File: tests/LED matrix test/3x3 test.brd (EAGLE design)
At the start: 100 x 80 mm, 21 parts

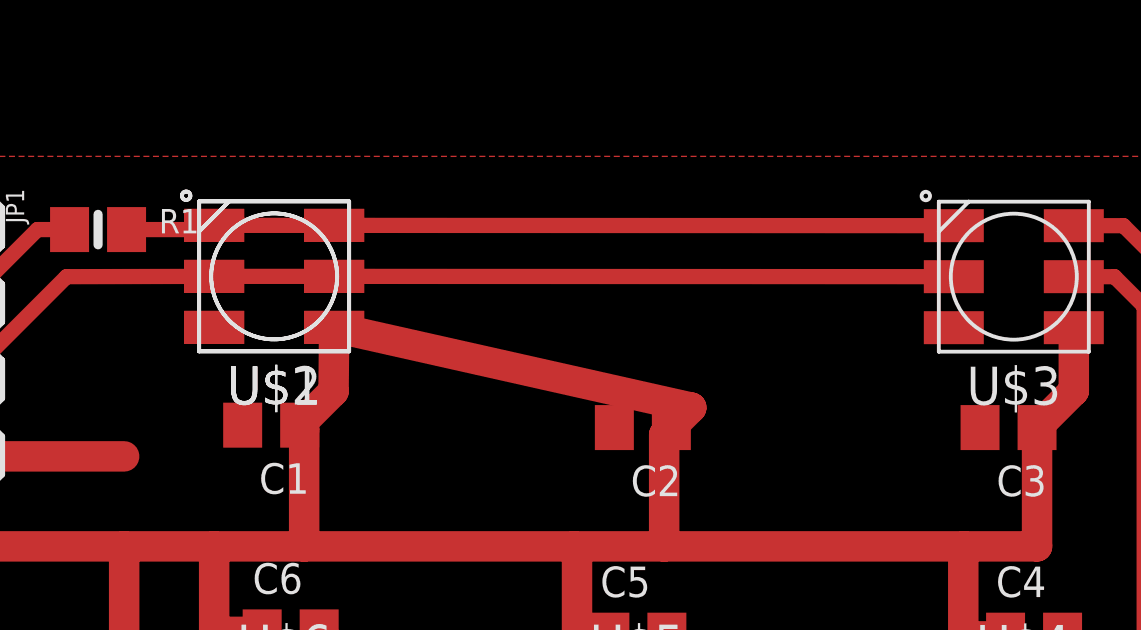
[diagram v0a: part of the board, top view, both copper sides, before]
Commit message: fix LED2 position
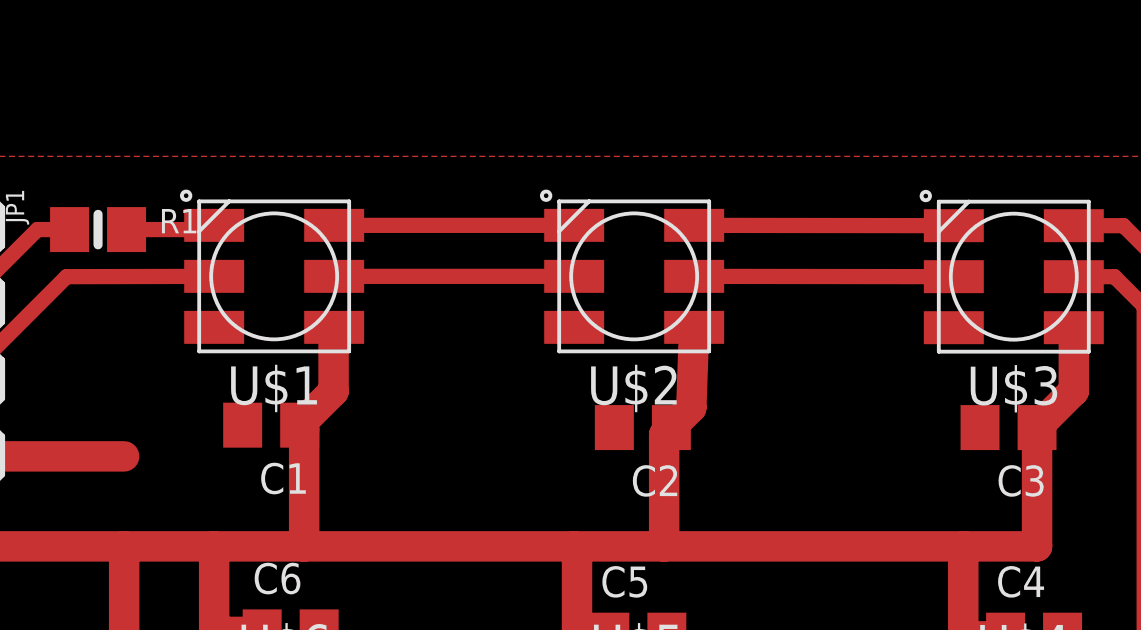
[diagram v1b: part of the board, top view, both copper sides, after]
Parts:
- moved U$2 12.0 mm to (50.0, 65.0)
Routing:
- net N$2: track 20.7 -> 8.66 mm
- net N$10: track 20.7 -> 8.66 mm
- net VCC: track 193.9 -> 184.4 mm
- net N$9: track 4.00 -> 8.00 mm
- net N$1: track 4.00 -> 8.00 mm
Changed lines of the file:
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@@
 <element name="C9" library="dp_devices" package="C805" value="" x="63.02" y="26.85" rot="R180"/>
 <element name="U$1" library="jos-ph" package="APA102_5050" value="APA1025050" x="38" y="65"/>
-<element name="U$2" library="jos-ph" package="APA102_5050" value="APA1025050" x="38" y="65"/>
+<element name="U$2" library="jos-ph" package="APA102_5050" value="APA1025050" x="50" y="65"/>
 <element name="U$3" library="jos-ph" package="APA102_5050" value="APA1025050" x="62.655" y="64.99"/>
 <element name="U$4" library="jos-ph" package="APA102_5050" value="APA1025050" x="62.97" y="49.11" rot="R180"/>
@@
 <contactref element="U$1" pad="3"/>
 <contactref element="U$2" pad="4"/>
-<wire x1="40" y1="66.7" x2="36" y2="66.7" width="0.508" layer="1"/>
+<wire x1="40" y1="66.7" x2="48" y2="66.7" width="0.508" layer="1"/>
 </signal>
 <signal name="N$2">
 <contactref element="U$2" pad="3"/>
 <contactref element="U$3" pad="4"/>
-<wire x1="40" y1="66.7" x2="60.655" y2="66.69" width="0.508" layer="1"/>
+<wire x1="52" y1="66.7" x2="60.655" y2="66.69" width="0.508" layer="1"/>
 </signal>
 <signal name="N$9">
 <contactref element="U$1" pad="2"/>
 <contactref element="U$2" pad="5"/>
-<wire x1="40" y1="65" x2="36" y2="65" width="0.508" layer="1"/>
+<wire x1="40" y1="65" x2="48" y2="65" width="0.508" layer="1"/>
 </signal>
 <signal name="N$10">
 <contactref element="U$2" pad="2"/>
 <contactref element="U$3" pad="5"/>
-<wire x1="40" y1="65" x2="60.655" y2="64.99" width="0.508" layer="1"/>
+<wire x1="52" y1="65" x2="60.655" y2="64.99" width="0.508" layer="1"/>
 </signal>
 <signal name="VCC">
@@
 <wire x1="62.38" y1="53.04" x2="62.34" y2="53" width="1.016" layer="1"/>
 <wire x1="62.34" y1="53" x2="60.97" y2="53" width="1.016" layer="1"/>
-<wire x1="39.98" y1="61.17" x2="38.85" y2="60.04" width="1.016" layer="1"/>
-<wire x1="39.98" y1="61.17" x2="40" y2="63.3" width="1.016" layer="1"/>
+<wire x1="38.85" y1="60.04" x2="39.98" y2="61.17" width="1.016" layer="1"/>
 <wire x1="51.905" y1="60.625" x2="51.24" y2="59.96" width="1.016" layer="1"/>
-<wire x1="51.905" y1="60.625" x2="40" y2="63.3" width="1.016" layer="1"/>
+<wire x1="51.905" y1="60.625" x2="52" y2="63.3" width="1.016" layer="1"/>
 <wire x1="63.43" y1="59.96" x2="64.655" y2="61.185" width="1.016" layer="1"/>
 <wire x1="64.655" y1="61.185" x2="64.655" y2="63.29" width="1.016" layer="1"/>
@@
 <wire x1="48.095" y1="53" x2="48.135" y2="53.04" width="1.016" layer="1"/>
 <wire x1="48.135" y1="53.04" x2="49.19" y2="53.04" width="1.016" layer="1"/>
+<wire x1="39.98" y1="61.17" x2="39.98" y2="63.28" width="1.016" layer="1"/>
+<wire x1="39.98" y1="63.28" x2="40" y2="63.3" width="1.016" layer="1"/>
 </signal>
 <signal name="GND">
